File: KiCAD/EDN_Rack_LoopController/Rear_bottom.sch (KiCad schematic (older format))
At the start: 35 parts, among them J15 AudioJack2_Switch, J16 AudioJack2_Switch, J17 AudioJack2_Switch, J18 AudioJack2_Switch, J19 From FX Send, J20 SW_CTRL2, J23 To FX Return, J5 AudioJack2_Switch, J6 AudioJack2_Switch, J7 AudioJack2_Switch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

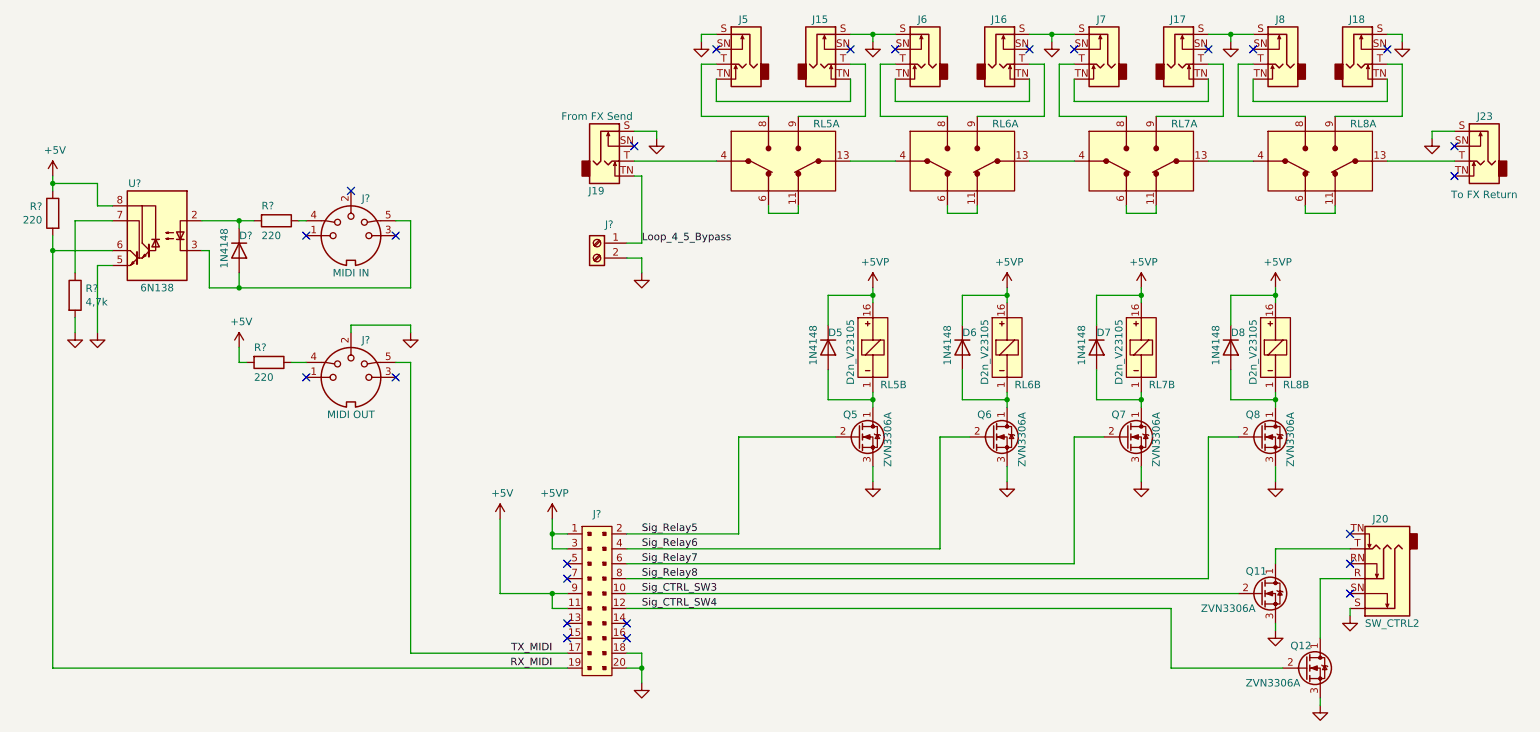
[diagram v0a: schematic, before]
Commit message: Schematic polish, added complete schematic pdf.
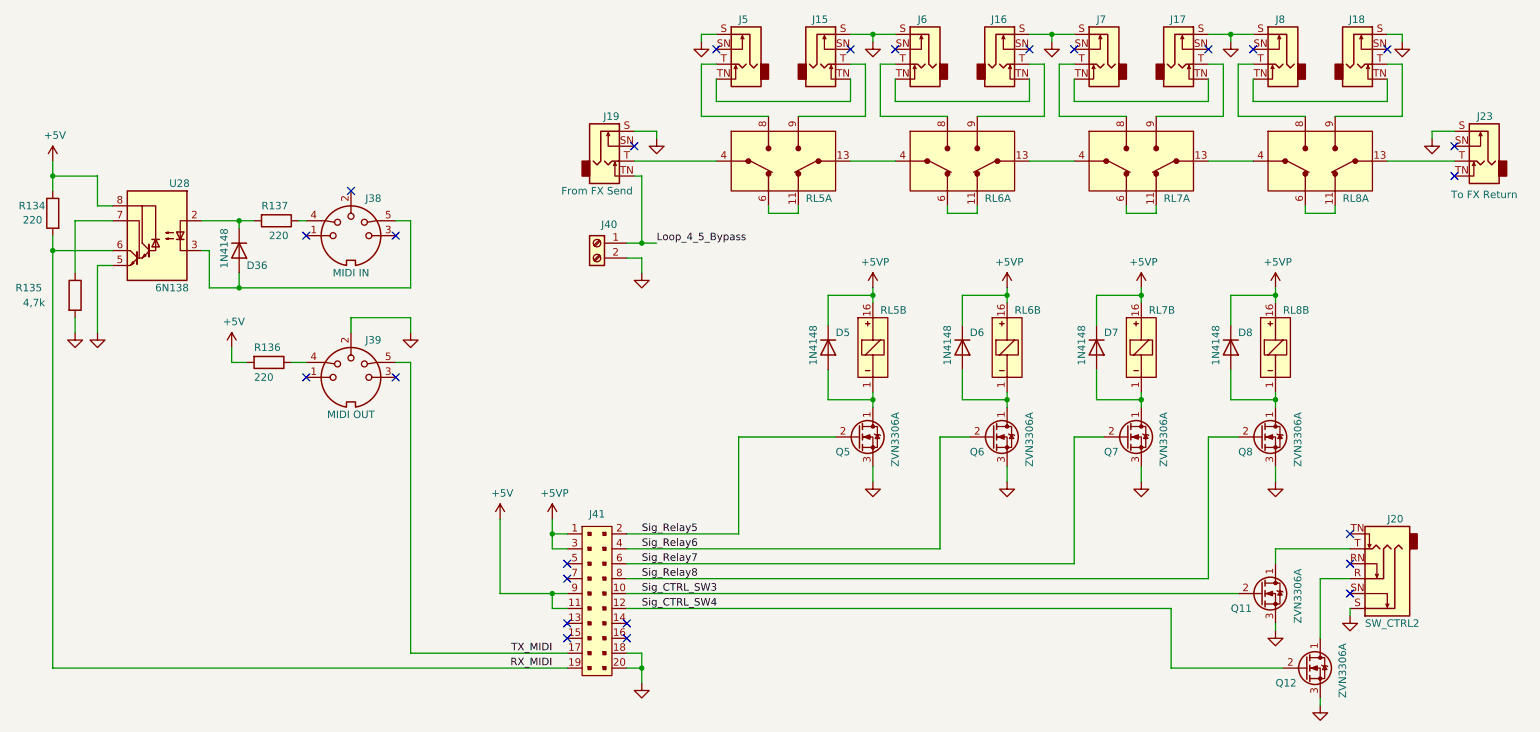
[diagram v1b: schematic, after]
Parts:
- gave numbers to parts that had none: 10
